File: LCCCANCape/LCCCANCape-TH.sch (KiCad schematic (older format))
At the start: 15 parts, among them J1 RJ45, J2 RJ45, P8 BeagleBone_Black_Header, P9 BeagleBone_Black_Header, T1 + 15 in -, T2 + 15 out -

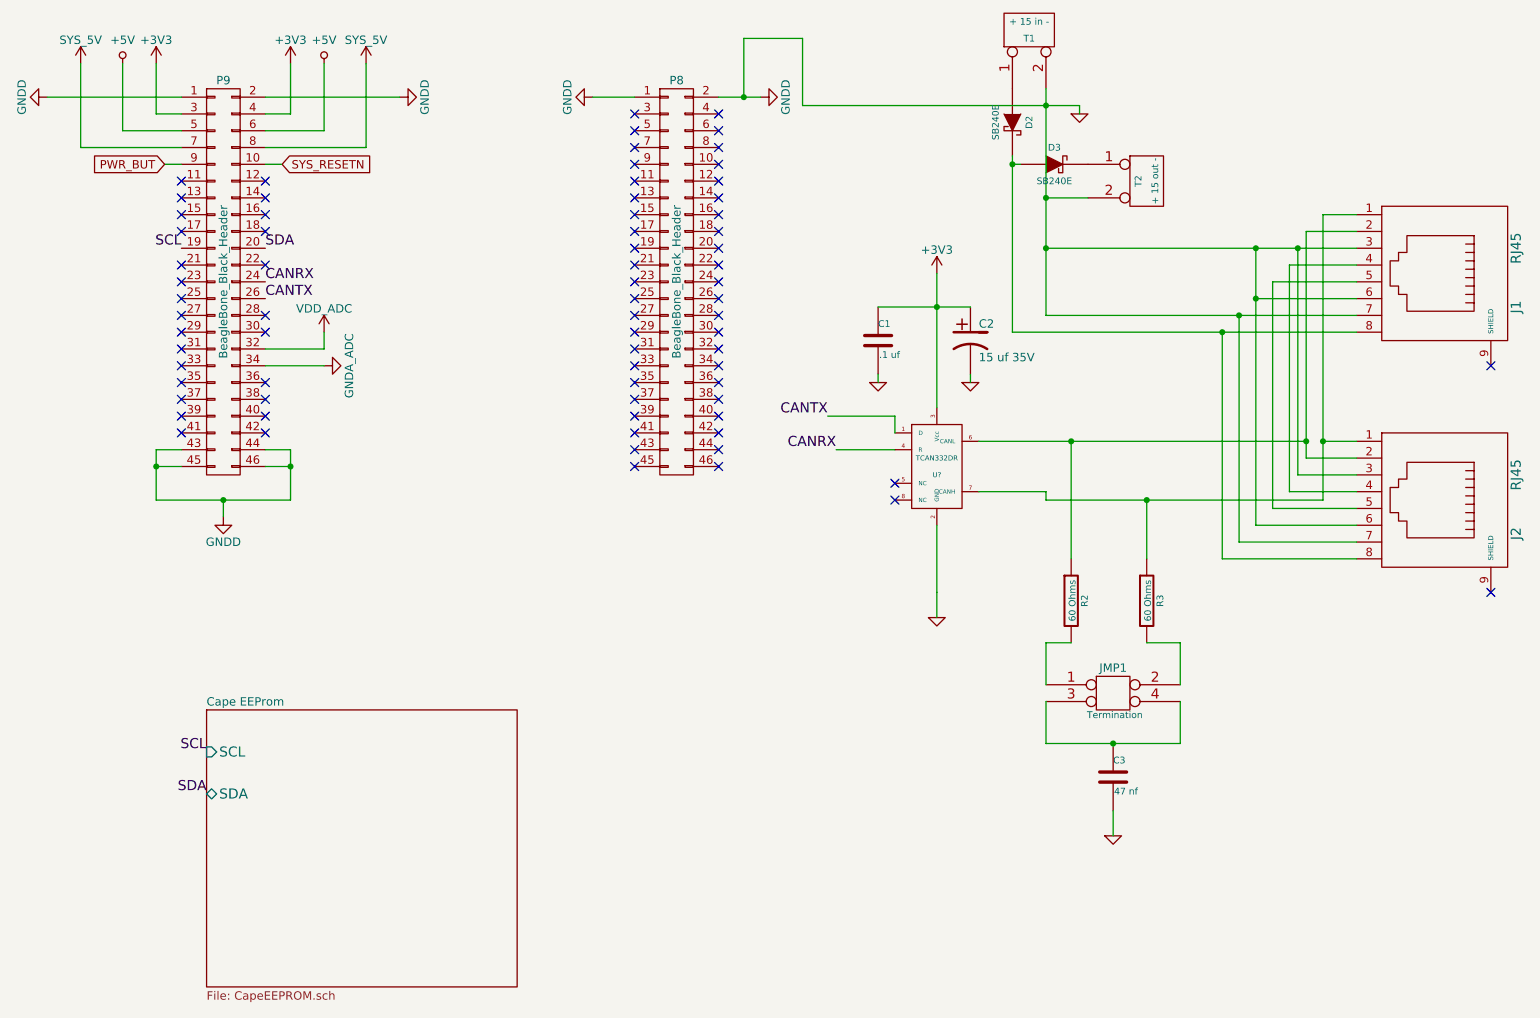
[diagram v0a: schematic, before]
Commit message: Updated LCCCANCape to use a TCAN332 (SMD) transceiver).  The Through Hole version is available still in the -TH.* files.
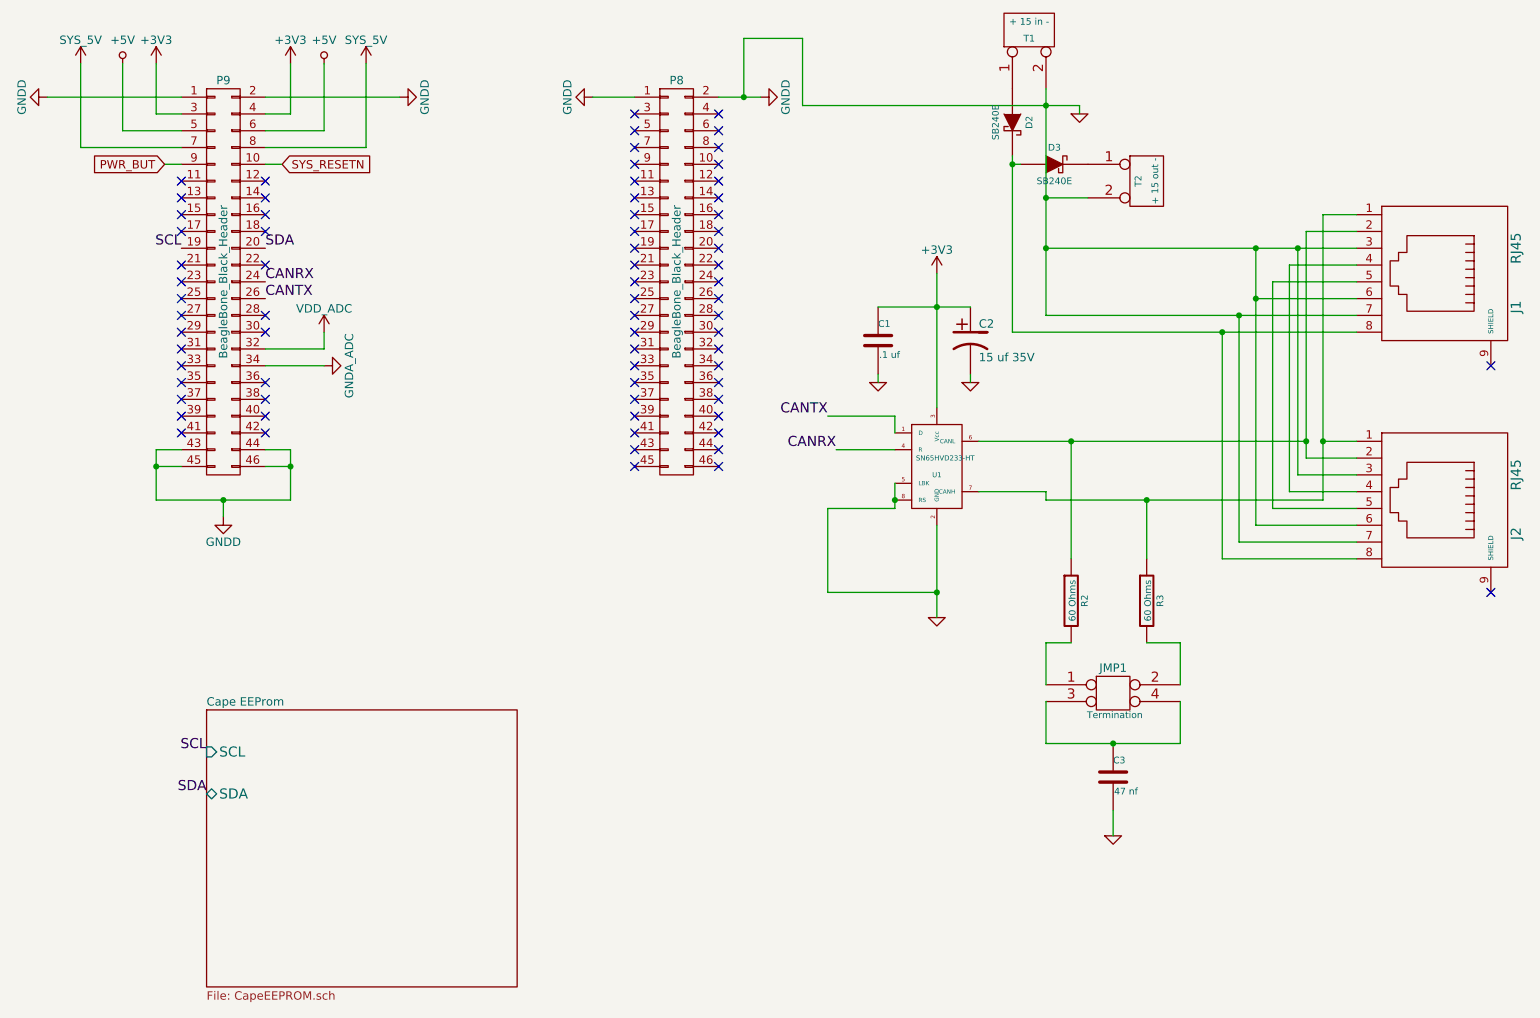
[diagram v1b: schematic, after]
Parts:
- removed U?: TCAN332DR, ~, symbol TCAN332DR
- added U1: SN65HVD233-HT, ~, symbol SN65HVD233-HT
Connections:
- net +3V3: now also U1.3 (Vcc)
- net CANRX: now also U1.4 (R)
- net CANTX: now also U1.1 (D)
- net GND: now also U1.2 (GND), U1.5 (LBK), U1.8 (RS)
- net at J1.1, J2.1, R3.1: now also U1.7 (CANH)
- net at J1.2, J2.2, R2.1: now also U1.6 (CANL)
- no-connect marks 74 -> 72
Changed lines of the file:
@@
 	2700 3250 2850 3250
 Wire Wire Line
-	2850 3250 2850 3350
-Wire Wire Line
-	2850 3350 2850 3550
-Wire Wire Line
-	2850 3550 2450 3550
-Wire Wire Line
-	2450 3550 2050 3550
-Wire Wire Line
-	2050 3550 2050 3350
-Wire Wire Line
-	2050 3350 2050 3250
+	2850 3250 2850 3550
+Wire Wire Line
+	2850 3550 2050 3550
+Wire Wire Line
+	2050 3550 2050 3250
 Wire Wire Line
 	2050 3250 2200 3250
@@
 	4650 1150 4900 1150
 Wire Wire Line
-	5400 1150 5550 1150
-Wire Wire Line
-	5550 1150 5650 1150
+	5400 1150 5650 1150
 Wire Wire Line
 	2700 2650 3050 2650
@@
 	2200 1550 2100 1550
 Wire Wire Line
-	7150 1500 7150 1550
-Wire Wire Line
-	7150 1550 7150 2550
+	7150 1500 7150 2550
 Wire Wire Line
 	7350 1750 7600 1750
 Wire Wire Line
-	7350 1100 7350 1200
-Wire Wire Line
-	7350 1200 7350 1750
-Wire Wire Line
-	7350 1750 7350 2050
-Wire Wire Line
-	7350 2050 7350 2450
+	7350 1100 7350 2450
 Wire Wire Line
 	7550 1200 7550 1250
 Wire Wire Line
-	5900 1200 7350 1200
-Wire Wire Line
-	7350 1200 7550 1200
+	5900 1200 7550 1200
 Connection ~ 7350 1200
 Wire Wire Line
 	9200 1850 9000 1850
 Wire Wire Line
-	9000 1850 9000 3200
-Wire Wire Line
-	9000 3200 9000 3550
+	9000 1850 9000 3550
 Wire Wire Line
 	9000 3200 9200 3200
@@
 	9200 1950 8900 1950
 Wire Wire Line
-	8900 1950 8900 3200
-Wire Wire Line
-	8900 3200 8900 3300
+	8900 1950 8900 3300
 Wire Wire Line
 	8900 3300 9200 3300
@@
 	8850 3400 8850 2050
 Wire Wire Line
-	7350 2050 8600 2050
-Wire Wire Line
-	8600 2050 8850 2050
-Wire Wire Line
-	8850 2050 9200 2050
+	7350 2050 9200 2050
 Wire Wire Line
 	9200 2150 8800 2150
@@
 	9200 2350 8600 2350
 Wire Wire Line
-	8600 2050 8600 2350
-Wire Wire Line
-	8600 2350 8600 3700
+	8600 2050 8600 3700
 Wire Wire Line
 	8600 3700 9200 3700
@@
 	8500 3800 8500 2450
 Wire Wire Line
-	7350 2450 8500 2450
-Wire Wire Line
-	8500 2450 9200 2450
-Wire Wire Line
-	7150 2550 8400 2550
-Wire Wire Line
-	8400 2550 9200 2550
+	7350 2450 9200 2450
+Wire Wire Line
+	7150 2550 9200 2550
 Wire Wire Line
 	8400 2550 8400 3900
@@
 Connection ~ 8600 2050
 Wire Wire Line
-	9000 3550 7950 3550
-Wire Wire Line
-	7950 3550 7350 3550
+	9000 3550 7350 3550
 Connection ~ 9000 3200
 Wire Wire Line
-	6950 3200 7500 3200
-Wire Wire Line
-	7500 3200 8900 3200
+	6950 3200 8900 3200
 Connection ~ 8900 3200
 Wire Wire Line
@@
 Connection ~ 5550 1150
 Wire Wire Line
-	6700 2200 6700 2400
-Wire Wire Line
-	6700 2400 6700 3000
+	6700 2200 6700 3000
 $Comp
 L CP1 C2
@@
 $EndComp
 Wire Wire Line
-	6350 2400 6700 2400
-Wire Wire Line
-	6700 2400 6900 2400
+	6350 2400 6900 2400
 Connection ~ 6700 2400
 $Comp
@@
 $EndComp
 Wire Wire Line
-	6700 3700 6700 4100
-Wire Wire Line
-	6700 4100 6700 4250
+	6700 3700 6700 4250
+Wire Wire Line
+	6050 3600 6050 4100
+Wire Wire Line
+	6050 4100 6700 4100
 Text Label 2700 2250 0    60   ~ 0
 CANRX
@@
 	8150 5000 8150 4750
 Wire Wire Line
-	7350 5000 7750 5000
-Wire Wire Line
-	7750 5000 8150 5000
+	7350 5000 8150 5000
 Wire Wire Line
 	7350 4750 7350 5000
@@
 Connection ~ 7150 1550
 $Comp
+L SN65HVD233-HT U1
+U 1 1 5C7A7F11
+P 6700 3350
+F 0 "U1" H 6700 3300 30  0000 C CNN
+F 1 "SN65HVD233-HT" H 6750 3400 30  0000 C CNN
+F 2 "~" H 6700 3350 60  0000 C CNN
+F 3 "~" H 6700 3350 60  0000 C CNN
+	1    6700 3350
+	1    0    0    -1
+$EndComp
+$Comp
 L +3V3 #PWR019
 U 1 1 5C7A82B0
@@
 	6450 3050 6050 3050
 Wire Wire Line
+	6450 3600 6050 3600
+Wire Wire Line
+	6450 3450 6450 3600
+Connection ~ 6450 3550
+Wire Wire Line
 	6950 3500 7350 3500
 Wire Wire Line
 	7350 3500 7350 3550
-$Comp
-L TCAN332DR U?
-U 1 1 5C7B1976
-P 6700 3350
-F 0 "U?" H 6700 3300 30  0000 C CNN
-F 1 "TCAN332DR" H 6700 3400 30  0000 C CNN
-F 2 "~" H 6700 3350 60  0000 C CNN
-F 3 "~" H 6700 3350 60  0000 C CNN
-	1    6700 3350
-	1    0    0    -1
-$EndComp
-NoConn ~ 6450 3450
-NoConn ~ 6450 3550
+Connection ~ 6700 4100
 $EndSCHEMATC
